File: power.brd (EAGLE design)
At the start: 85 x 75 mm, 26 parts

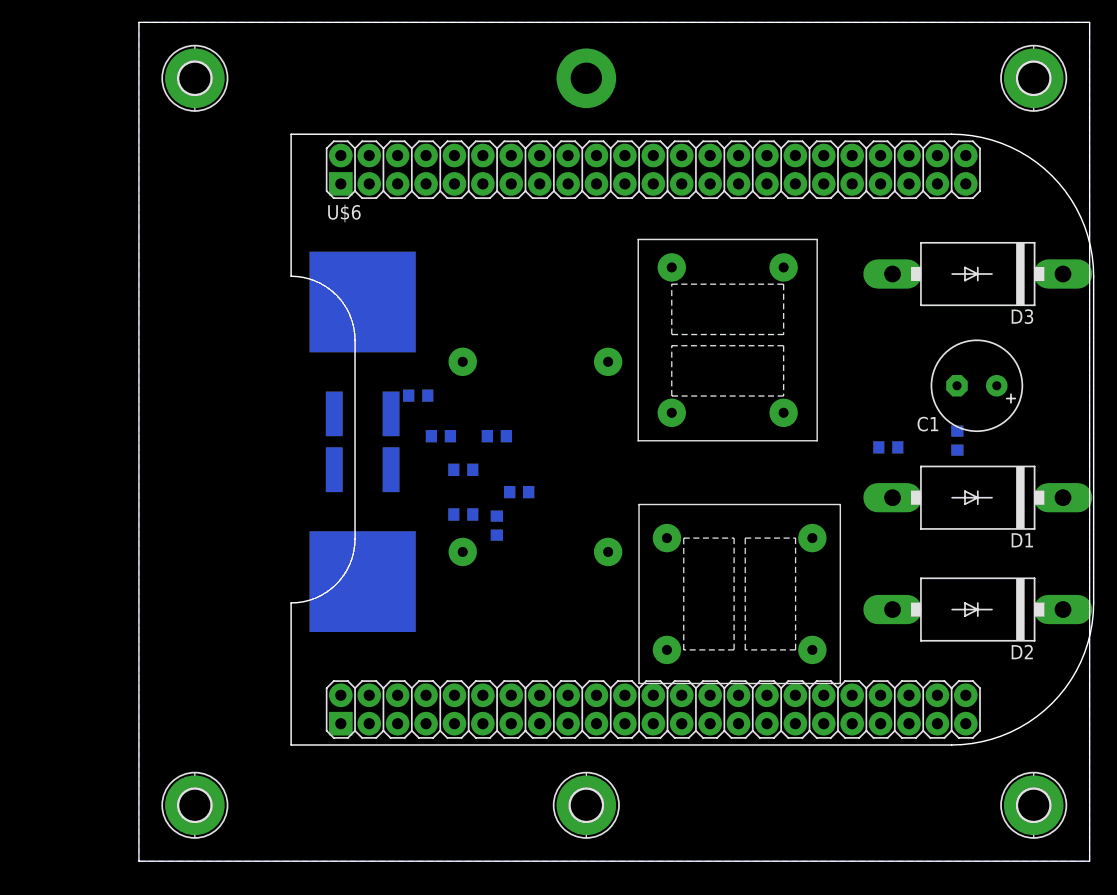
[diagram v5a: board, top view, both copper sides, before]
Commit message: schematic might be correct.  board is routed.  no idea if it's routed well.
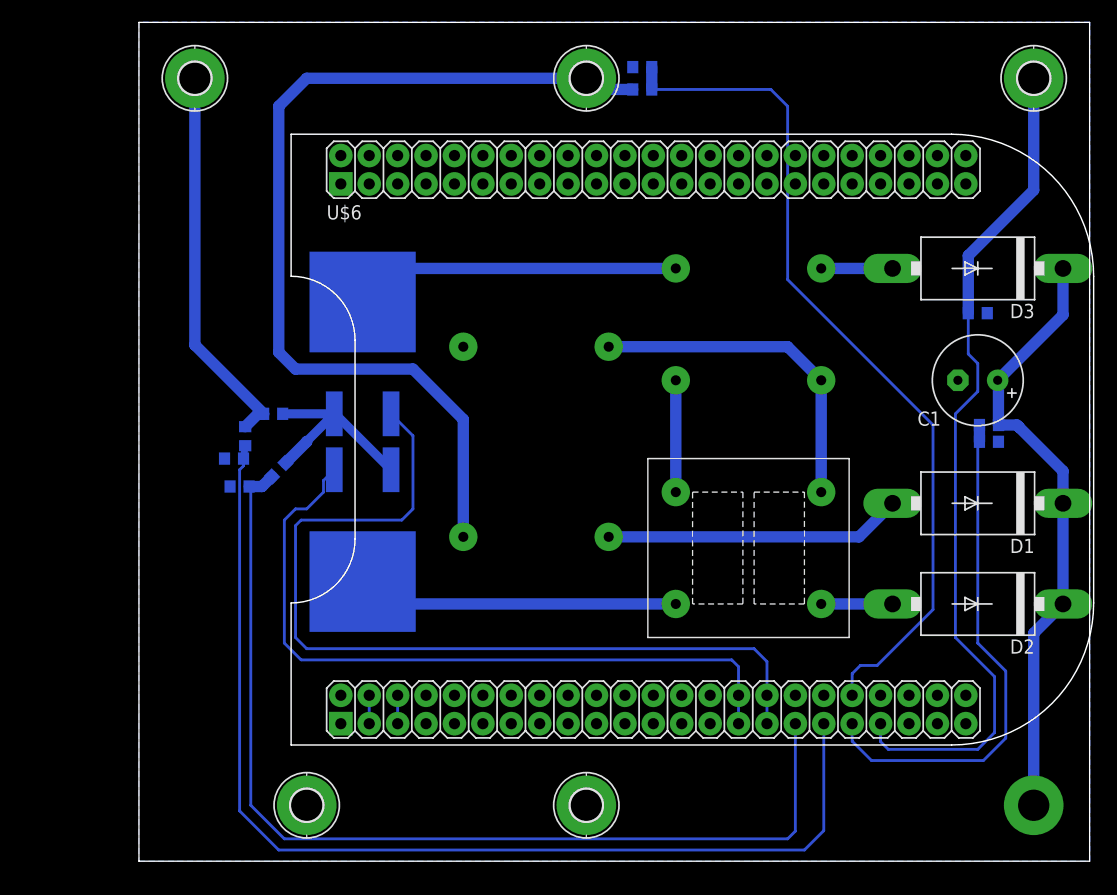
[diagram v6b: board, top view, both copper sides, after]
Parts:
- moved BAT+ 76.3 mm to (80.0, 5.00)
- moved H1 65.8 mm to (15.0, 5.00)
- moved PV+ 65.0 mm to (40.0, 70.0)
- moved PV- 65.0 mm to (5.00, 70.0)
- moved R4 43.0 mm to (45.0, 71.0), turned to 180 degrees
- moved R3 41.2 mm to (45.0, 69.0)
- moved H2 40.0 mm to (40.0, 5.00)
- moved R10 25.0 mm to (9.00, 33.5), turned to 180 degrees
- moved R6 23.6 mm to (8.50, 36.0), turned to 180 degrees
- moved R5 17.5 mm to (9.50, 38.0), turned to 270 degrees
- moved R9 16.5 mm to (12.5, 35.0), turned to 315 degrees
- moved R2 13.1 mm to (12.0, 40.0), turned to 180 degrees
- moved R1 11.5 mm to (75.0, 49.0), turned to 0 degrees
- moved R8 10.1 mm to (76.0, 37.5)
- moved R7 9.22 mm to (76.0, 39.0)
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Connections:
- removed net N$14: BAT-.B2,8, R1.2, U$6.83
- net N$10: now also U$6.83; no longer U$6.84
- net N$11: now also U$2.P$1, U$6.77; no longer R2.2, U$1.P$2, U$2.P$2
- net N$12: now also BAT-.B2,8, R1.2, U$6.85; no longer U$1.P$1, U$6.77
- net N$13: now also U$1.P$1; no longer U$2.P$1
- net N$17: now also U$6.81; no longer U$6.86
- net N$4: now also U$6.84; no longer U$6.85
- net N$8: now also R2.2, U$1.P$2, U$2.P$2
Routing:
- net N$17: track 0.00 -> 97.0 mm
- net N$18: track 0.00 -> 91.5 mm
- net N$3: track 0.00 -> 84.6 mm
- net N$11: track 0.00 -> 79.0 mm
- net N$4: track 0.00 -> 76.7 mm
- net N$12: track 0.00 -> 76.3 mm
- net N$13: track 0.00 -> 64.5 mm
- net N$7: track 0.00 -> 54.9 mm
- net N$10: track 0.00 -> 45.9 mm
- net N$16: track 0.00 -> 34.7 mm
- net N$6: track 0.00 -> 30.2 mm
- net N$5: track 0.00 -> 29.2 mm
- net N$15: track 0.00 -> 28.8 mm
- net N$1: track 0.00 -> 26.6 mm
- net N$8: track 0.00 -> 18.0 mm
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
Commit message: better ground paths
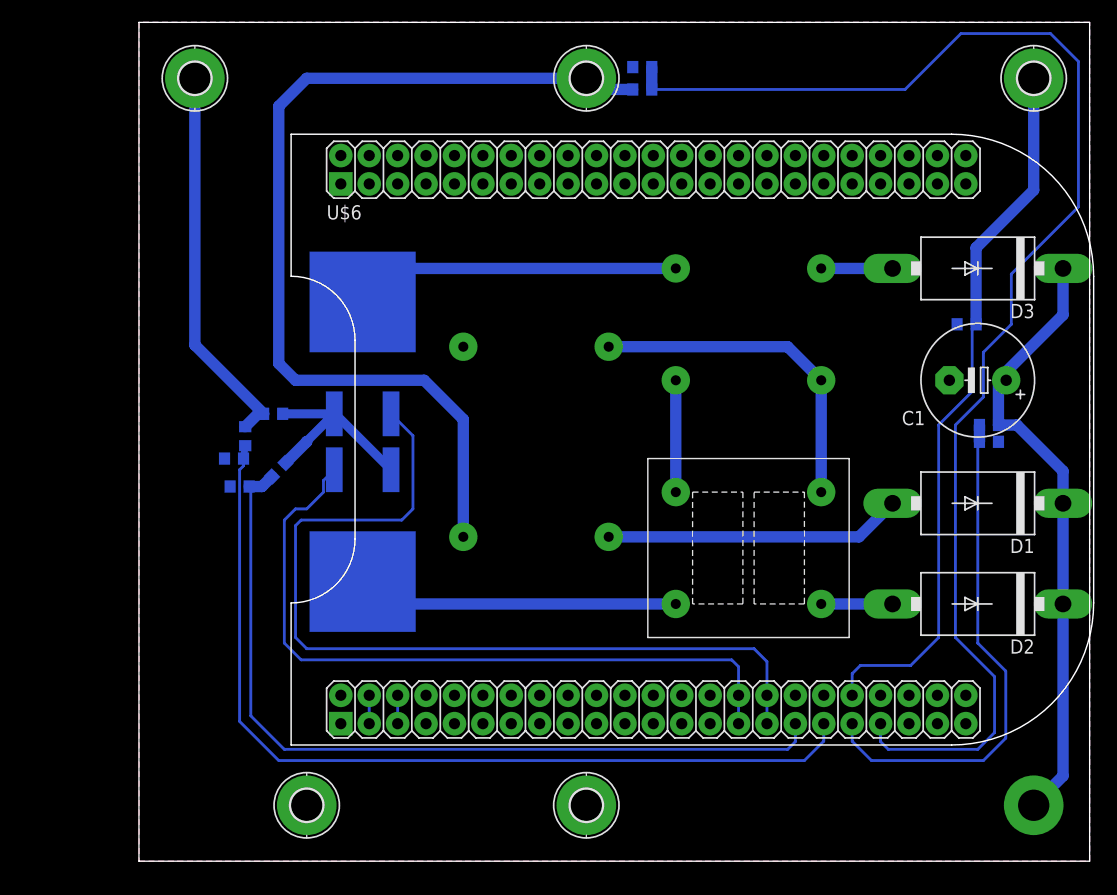
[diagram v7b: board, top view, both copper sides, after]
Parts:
- C1: device rcl:E3,5-8 -> rcl:E5-10,5
- moved R1 1.41 mm to (74.0, 48.0), turned to 180 degrees
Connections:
- net N$12: now also R3.2, R4.2; no longer BAT-.B2,8, R1.2
- net N$4: now also BAT-.B2,8, R1.2; no longer R3.2, R4.2
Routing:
- net N$12: track 76.3 -> 122.0 mm
- net N$18: track 91.5 -> 75.5 mm
- net N$17: track 97.0 -> 81.0 mm
- net N$4: track 76.7 -> 64.5 mm
- net N$3: track 84.6 -> 85.2 mm
- added copper zone on layer 1, net GND

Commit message: fixed a lot of things.  confidence that this could work is up to 1%.
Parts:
- removed H2: MOUNT-PAD-ROUND2.8, holes:2,8-PAD
- removed R7: 15k, rcl:R0603
- removed U$1, U$2: FDB6670AL, mjg:TO-263AB
- added U$7, U$8: 45NO6LG, semiconductors:D2PAK-3
- moved H1 10.0 mm to (5.00, 5.00)
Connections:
- net GND: no longer H2.B2,8
- net N$10: no longer R7.2
- net N$11: now also U$6.75, U$8.1; no longer U$2.P$1, U$6.77
- net N$13: now also U$6.77, U$7.1; no longer U$1.P$1, U$6.75
- net N$15: now also U$7.4; no longer U$1.P$3
- net N$5: now also U$8.4; no longer U$2.P$3
- net N$7: no longer R7.1
- net N$8: now also U$8.3; no longer U$1.P$2, U$2.P$2
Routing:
- net N$13: track 64.5 -> 73.2 mm
- net N$8: track 18.0 -> 11.4 mm
- net N$17: track 81.0 -> 84.5 mm
- net N$18: track 75.5 -> 78.6 mm
- net N$11: track 79.0 -> 76.9 mm
- net N$10: track 45.9 -> 44.4 mm
- net N$5: track 29.2 -> 27.9 mm
- net N$7: track 55.2 -> 54.0 mm
- net N$3: track 85.2 -> 86.0 mm
- net N$15: track 28.8 -> 28.1 mm
